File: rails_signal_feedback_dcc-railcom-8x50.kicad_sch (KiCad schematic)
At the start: 8 parts, among them Q101 S8550, Q102 S8050, Q103 S8050, Q104 S8550

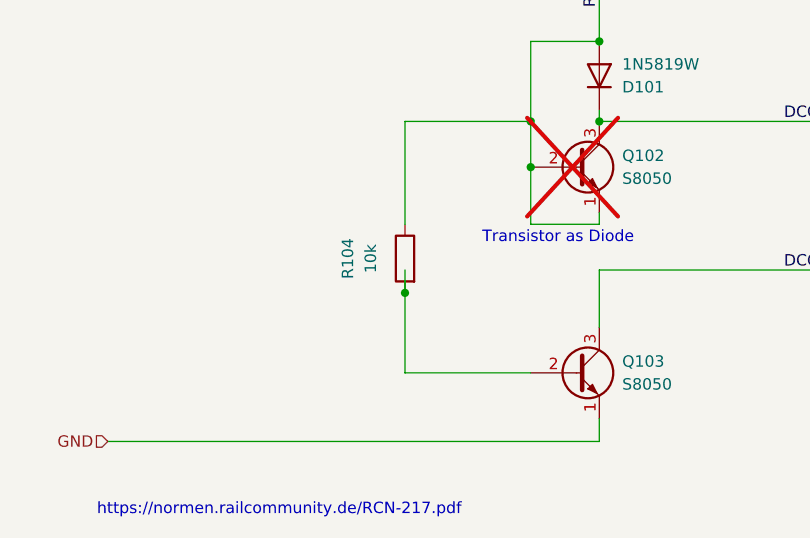
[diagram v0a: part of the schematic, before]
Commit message: Chg - Clearer PCB layout
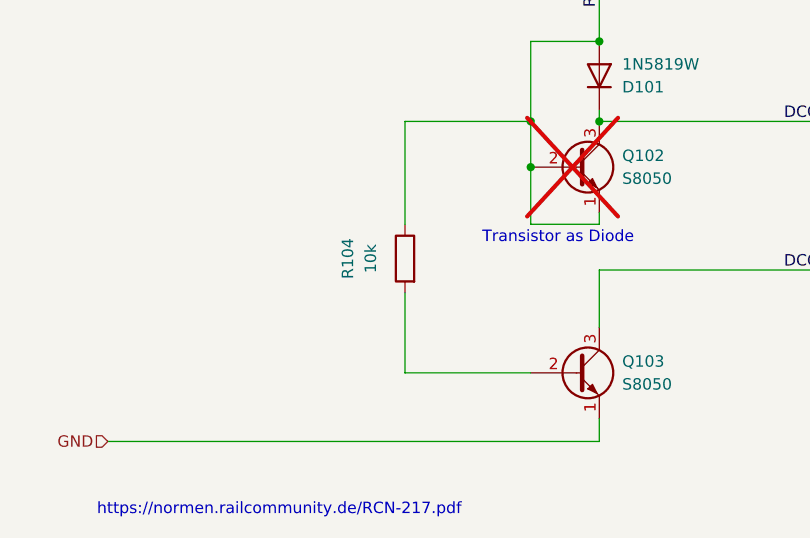
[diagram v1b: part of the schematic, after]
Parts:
- R101, R102, R104: footprint Resistor_SMD:R_0603_1608Metric_Pad0.98x0.95mm_HandSolder -> Resistor_SMD:R_0603_1608Metric
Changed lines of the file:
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@@
-	)
-	(junction
-		(at 82.55 114.3)
-		(diameter 0)
-		(color 0 0 0 0)
 	)
 	(junction
@@
 		(pts
 			(xy 104.14 86.36) (xy 96.52 86.36)
-		)
-		(stroke
-			(width 0)
-			(type default)
-		)
-	)
-	(wire
-		(pts
-			(xy 82.55 111.76) (xy 82.55 114.3)
 		)
 		(stroke
@@
 			(project "rails_signal_feedback_dcc-railcom-8x50"
 				(path "/6d7aefd8-fcb8-4935-b99c-c7045c3b702f"
-					(reference "Q101")
-					(unit 1)
-				)
-				(path "/6d7aefd8-fcb8-4935-b99c-c7045c3b702f/2444bbf9-5682-4e11-b667-350d7de8ca4f"
 					(reference "Q101")
 					(unit 1)
@@
 					(unit 1)
 				)
-				(path "/6d7aefd8-fcb8-4935-b99c-c7045c3b702f/2444bbf9-5682-4e11-b667-350d7de8ca4f"
-					(reference "Q104")
-					(unit 1)
-				)
 			)
 			(project "xDuinoRail-Arduino-RailcomDetect-Dev"
@@
 			)
 		)
-		(property "Footprint" "Resistor_SMD:R_0603_1608Metric_Pad0.98x0.95mm_HandSolder"
+		(property "Footprint" "Resistor_SMD:R_0603_1608Metric"
 			(at 102.362 49.53 90)
 			(effects
@@
 			(project "rails_signal_feedback_dcc-railcom-8x50"
 				(path "/6d7aefd8-fcb8-4935-b99c-c7045c3b702f"
-					(reference "R102")
-					(unit 1)
-				)
-				(path "/6d7aefd8-fcb8-4935-b99c-c7045c3b702f/2444bbf9-5682-4e11-b667-350d7de8ca4f"
 					(reference "R102")
 					(unit 1)
@@
 					(unit 1)
 				)
-				(path "/6d7aefd8-fcb8-4935-b99c-c7045c3b702f/2444bbf9-5682-4e11-b667-350d7de8ca4f"
-					(reference "Q102")
-					(unit 1)
-				)
 			)
 			(project "xDuinoRail-Arduino-RailcomDetect-Dev"
@@
 			)
 		)
-		(property "Footprint" "Resistor_SMD:R_0603_1608Metric_Pad0.98x0.95mm_HandSolder"
+		(property "Footprint" "Resistor_SMD:R_0603_1608Metric"
 			(at 73.66 65.532 90)
 			(effects
@@
 			(project "rails_signal_feedback_dcc-railcom-8x50"
 				(path "/6d7aefd8-fcb8-4935-b99c-c7045c3b702f"
-					(reference "R101")
-					(unit 1)
-				)
-				(path "/6d7aefd8-fcb8-4935-b99c-c7045c3b702f/2444bbf9-5682-4e11-b667-350d7de8ca4f"
 					(reference "R101")
 					(unit 1)
@@
 			(project "rails_signal_feedback_dcc-railcom-8x50"
 				(path "/6d7aefd8-fcb8-4935-b99c-c7045c3b702f"
-					(reference "Q103")
-					(unit 1)
-				)
-				(path "/6d7aefd8-fcb8-4935-b99c-c7045c3b702f/2444bbf9-5682-4e11-b667-350d7de8ca4f"
 					(reference "Q103")
 					(unit 1)
@@
 			)
 		)
-		(property "Footprint" "Resistor_SMD:R_0603_1608Metric_Pad0.98x0.95mm_HandSolder"
+		(property "Footprint" "Resistor_SMD:R_0603_1608Metric"
 			(at 84.328 110.49 90)
 			(effects
@@
 			(project "rails_signal_feedback_dcc-railcom-8x50"
 				(path "/6d7aefd8-fcb8-4935-b99c-c7045c3b702f"
-					(reference "R104")
-					(unit 1)
-				)
-				(path "/6d7aefd8-fcb8-4935-b99c-c7045c3b702f/2444bbf9-5682-4e11-b667-350d7de8ca4f"
 					(reference "R104")
 					(unit 1)
@@
 					(reference "D101")
 					(unit 1)
-				)
-				(path "/6d7aefd8-fcb8-4935-b99c-c7045c3b702f/2444bbf9-5682-4e11-b667-350d7de8ca4f"
-					(reference "D101")
-					(unit 1)
